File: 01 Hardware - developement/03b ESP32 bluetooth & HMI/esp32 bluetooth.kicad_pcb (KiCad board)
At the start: 2 copper layers, 152.4 x 142.2 mm, 115 parts, among them J1 I2C, J2 UART, J3 power supply, J4 Jtag, J5 I2S, J6 Backlight and leds, J7 to stepper motor, J8 Conn_01x01_Pin, Q1 BC817, Q2 BSS138, Q3 BSS138, Q4 BSS138, SW1 SW_Push_Dual, SW10 Strapping button, SW2 SW_Push_Dual, SW3 SW_Push_Dual, SW4 SW_Push_Dual, SW5 SW_Push_Dual, SW6 Rotary_Encoder_Switch, SW7 Rotary_Encoder_Switch, SW8 Strapping button, SW9 Strapping button, U1 DRV8825_STEPPER_MOTOR_DRIVER_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, U2 ESP32-DevKitC, U3 MCP23008

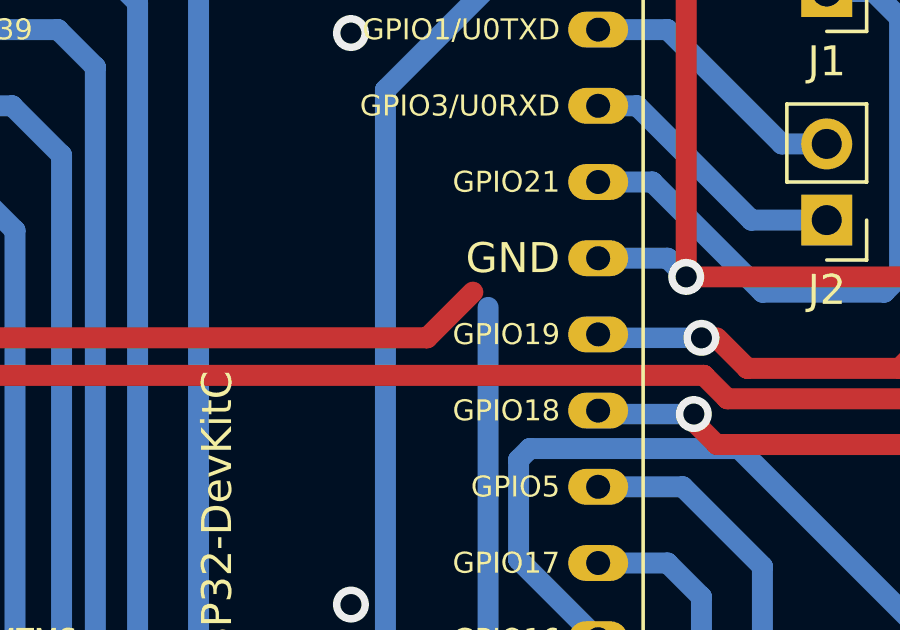
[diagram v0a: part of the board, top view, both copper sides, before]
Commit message: hw and esp32 fw inprovements GOLDEN SAMPLE, restore point
- hw - poprawiono footprinty modułów i zamieniono mux select na power supply sustain pin
- fw - poprawiono kalsę StepperOptoPowerOFF
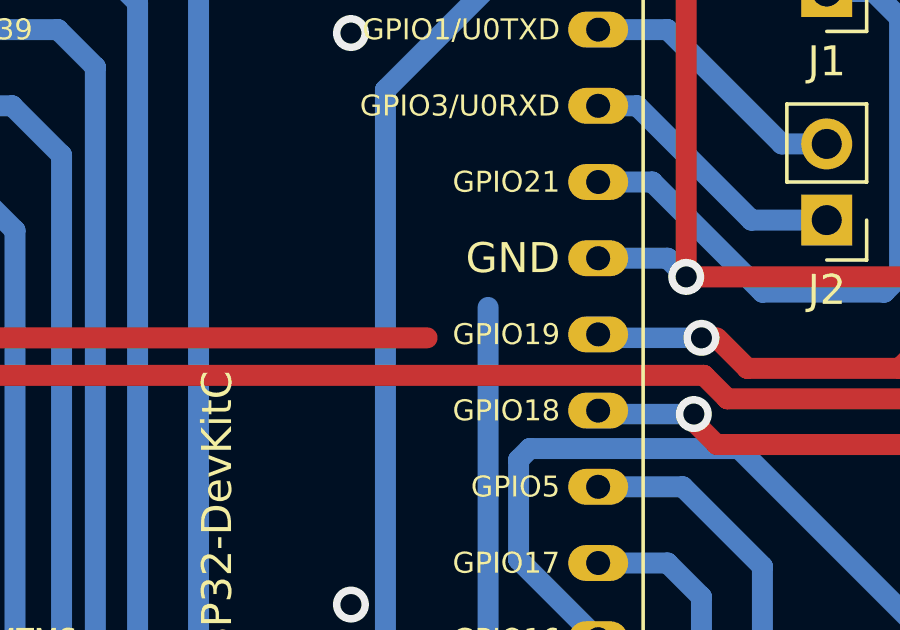
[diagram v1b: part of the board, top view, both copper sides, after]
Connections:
- net /MUX_select renamed /~{PS_Sust_ESP32}
- J5 pad 4: /I2S_MCLK -> unconnected-(J5-Pin_4-Pad4)
- J8 pad 1: Net-(J8-Pin_1) -> unconnected-(J8-Pin_1-Pad1)
- R52 pad 2: Net-(J8-Pin_1) -> unconnected-(J8-Pin_1-Pad1)
- U3 pad 8: Net-(J8-Pin_1) -> unconnected-(J8-Pin_1-Pad1)
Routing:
- net /I2S_MCLK: track 37.1 -> 0.00 mm, vias 1 -> 0
- net unconnected-(J5-Pin_4-Pad4): track 0.00 -> 34.9 mm, vias 0 -> 1
- net unconnected-(J8-Pin_1-Pad1): track 0.00 -> 11.5 mm
- net Net-(J8-Pin_1): track 11.5 -> 0.00 mm
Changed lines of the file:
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@@
   (net 19 "/I2C0_SDA")
   (net 20 "/I2C0_SCL")
-  (net 21 "/I2S_MCLK")
+  (net 21 "unconnected-(J5-Pin_4-Pad4)")
   (net 22 "/BT_UATR_RX")
   (net 23 "/BT_UATR_TX")
@@
   (net 35 "/I2S_LRCLK")
   (net 36 "/BOOT")
-  (net 37 "/MUX_select")
+  (net 37 "/~{PS_Sust_ESP32}")
   (net 38 "+5V")
   (net 39 "Net-(J6-Pin_3)")
@@
   (net 61 "Net-(R33-Pad2)")
   (net 62 "Net-(R35-Pad2)")
-  (net 63 "Net-(J8-Pin_1)")
+  (net 63 "unconnected-(J8-Pin_1-Pad1)")
   (net 64 "Net-(R39-Pad2)")
   (net 65 "/~{MotorSleep}")
@@
       (net 35 "/I2S_LRCLK") (pinfunction "Pin_3") (pintype "passive"))
     (pad "4" thru_hole oval (at 0 7.62) (size 1.7 1.7) (drill 1) (layers "*.Cu" "*.Mask")
-      (net 21 "/I2S_MCLK") (pinfunction "Pin_4") (pintype "passive"))
+      (net 21 "unconnected-(J5-Pin_4-Pad4)") (pinfunction "Pin_4") (pintype "passive+no_connect"))
     (pad "5" thru_hole oval (at 0 10.16) (size 1.7 1.7) (drill 1) (layers "*.Cu" "*.Mask")
-      (net 37 "/MUX_select") (pinfunction "Pin_5") (pintype "passive"))
+      (net 37 "/~{PS_Sust_ESP32}") (pinfunction "Pin_5") (pintype "passive"))
     (model "${KICAD6_3DMODEL_DIR}/Connector_PinHeader_2.54mm.3dshapes/PinHeader_1x05_P2.54mm_Vertical.wrl"
       (offset (xyz 0 0 0))
@@
       (net 91 "unconnected-(U3-NC-Pad7)") (pinfunction "NC") (pintype "no_connect"))
     (pad "8" smd roundrect (at -4.65 3.81) (size 2.05 0.6) (layers "F.Cu" "F.Paste" "F.Mask") (roundrect_rratio 0.25)
-      (net 63 "Net-(J8-Pin_1)") (pinfunction "INT") (pintype "output"))
+      (net 63 "unconnected-(J8-Pin_1-Pad1)") (pinfunction "INT") (pintype "output"))
     (pad "9" smd roundrect (at -4.65 5.08) (size 2.05 0.6) (layers "F.Cu" "F.Paste" "F.Mask") (roundrect_rratio 0.25)
       (net 2 "GNDD") (pinfunction "VSS") (pintype "power_in"))
     (pad "10" smd roundrect (at 4.65 5.08) (size 2.05 0.6) (layers "F.Cu" "F.Paste" "F.Mask") (roundrect_rratio 0.25)
-      (net 85 "unconnected-(U3-GP0-Pad10)") (pinfunction "GP0") (pintype "bidirectional"))
+      (net 85 "unconnected-(U3-GP0-Pad10)") (pinfunction "GP0") (pintype "bidirectional+no_connect"))
     (pad "11" smd roundrect (at 4.65 3.81) (size 2.05 0.6) (layers "F.Cu" "F.Paste" "F.Mask") (roundrect_rratio 0.25)
       (net 84 "Net-(U3-GP1)") (pinfunction "GP1") (pintype "bidirectional"))
@@
       (stroke (width 0.1) (type solid)) (layer "F.Fab"))
     (pad "1" thru_hole rect (at 0 0) (size 1.7 1.7) (drill 1) (layers "*.Cu" "*.Mask")
-      (net 63 "Net-(J8-Pin_1)") (pinfunction "Pin_1") (pintype "passive"))
+      (net 63 "unconnected-(J8-Pin_1-Pad1)") (pinfunction "Pin_1") (pintype "passive"))
     (model "${KICAD6_3DMODEL_DIR}/Connector_PinHeader_2.54mm.3dshapes/PinHeader_1x01_P2.54mm_Vertical.wrl"
       (offset (xyz 0 0 0))
@@
       (net 47 "+3V3") (pintype "passive"))
     (pad "2" smd roundrect (at 0.825 0 180) (size 0.8 0.95) (layers "B.Cu" "B.Paste" "B.Mask") (roundrect_rratio 0.25)
-      (net 63 "Net-(J8-Pin_1)") (pintype "passive"))
+      (net 63 "unconnected-(J8-Pin_1-Pad1)") (pintype "passive"))
     (model "${KICAD6_3DMODEL_DIR}/Resistor_SMD.3dshapes/R_0603_1608Metric.wrl"
       (offset (xyz 0 0 0))
@@
       (net 84 "Net-(U3-GP1)") (pintype "passive"))
     (pad "2" smd roundrect (at 0.825 0 180) (size 0.8 0.95) (layers "B.Cu" "B.Paste" "B.Mask") (roundrect_rratio 0.25)
-      (net 37 "/MUX_select") (pintype "passive"))
+      (net 37 "/~{PS_Sust_ESP32}") (pintype "passive"))
     (model "${KICAD6_3DMODEL_DIR}/Resistor_SMD.3dshapes/R_0603_1608Metric.wrl"
       (offset (xyz 0 0 0))
@@
   (segment (start 111.875 86.245) (end 113.145 84.975) (width 0.7) (layer "B.Cu") (net 20))
   (segment (start 109.84 86.245) (end 111.875 86.245) (width 0.7) (layer "B.Cu") (net 20))
-  (segment (start 105.664 97.536) (end 104.14 99.06) (width 0.7) (layer "F.Cu") (net 21))
   (segment (start 104.14 99.06) (end 88.9 99.06) (width 0.7) (layer "F.Cu") (net 21))
   (segment (start 87.503 97.663) (end 74.803 97.663) (width 0.7) (layer "F.Cu") (net 21))

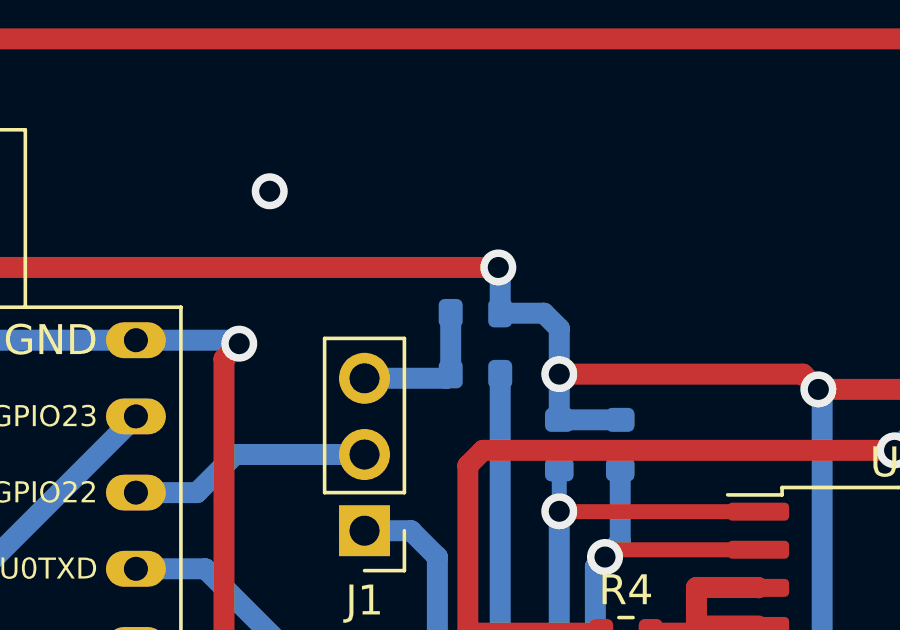
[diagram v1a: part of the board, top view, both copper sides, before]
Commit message: ESP32 bluetooth & HMI -HW- interrupt request pull-down
Zmieniono R57 - pierwotnie rezystor ten był PULL-UP na linii i2cItterrupt request teraz jest PULL-DOWN
Zmiana jest po to, aby wykryć start ESp32. Po zboot'owaniu się ESP32 gaje sygnał na tej linii UP
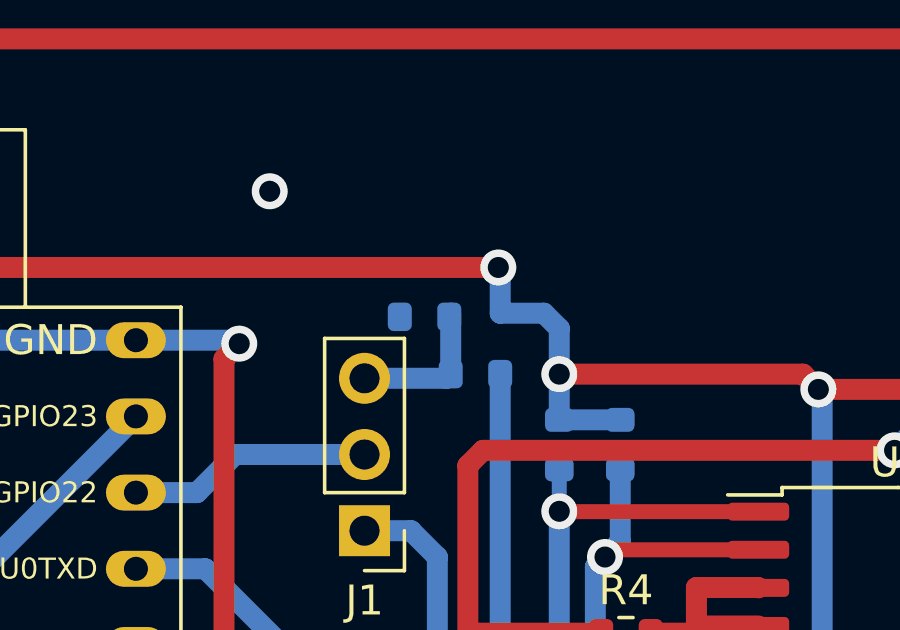
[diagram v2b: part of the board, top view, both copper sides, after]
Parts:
- moved R57 1.70 mm to (119.5, 80.4), turned to 180 degrees
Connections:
- R57 pad 2: +3V3 -> GNDD
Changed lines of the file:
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@@
   )
   (footprint "Resistor_SMD:R_0603_1608Metric" (layer "B.Cu")
-    (at 121.158 80.264)
+    (at 119.460595 80.384893 180)
     (descr "Resistor SMD 0603 (1608 Metric), square (rectangular) end terminal, IPC_7351 nominal, (Body size source: IPC-SM-782 page 72, https://www.pcb-3d.com/wordpress/wp-content/uploads/ipc-sm-782a_amendment_1_and_2.pdf), generated with kicad-footprint-generator")
     (tags "resistor")
@@
     (fp_line (start 0.8 0.4125) (end 0.8 -0.4125)
       (stroke (width 0.1) (type solid)) (layer "B.Fab"))
-    (pad "1" smd roundrect (at -0.825 0) (size 0.8 0.95) (layers "B.Cu" "B.Paste" "B.Mask") (roundrect_rratio 0.25)
+    (pad "1" smd roundrect (at -0.825 0 180) (size 0.8 0.95) (layers "B.Cu" "B.Paste" "B.Mask") (roundrect_rratio 0.25)
       (net 95 "Net-(J1-Pin_3)") (pintype "passive"))
-    (pad "2" smd roundrect (at 0.825 0) (size 0.8 0.95) (layers "B.Cu" "B.Paste" "B.Mask") (roundrect_rratio 0.25)
-      (net 47 "+3V3") (pintype "passive"))
+    (pad "2" smd roundrect (at 0.825 0 180) (size 0.8 0.95) (layers "B.Cu" "B.Paste" "B.Mask") (roundrect_rratio 0.25)
+      (net 2 "GNDD") (pintype "passive"))
     (model "${KICAD6_3DMODEL_DIR}/Resistor_SMD.3dshapes/R_0603_1608Metric.wrl"
       (offset (xyz 0 0 0))

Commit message: Do poprwy jest schemat rotary encodera
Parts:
- added D10: ESD5Z3.3T1G, Diode_SMD:D_SOD-523, F.Cu at (-64.0, 106.2)
- added D11: ESD5Z3.3T1G, Diode_SMD:D_SOD-523, F.Cu at (-64.0, 108.7)
- added D12: ESD5Z3.3T1G, Diode_SMD:D_SOD-523, F.Cu at (-64.0, 111.1)
- added D5: ESD5Z3.3T1G, Diode_SMD:D_SOD-523, F.Cu at (-64.0, 94.0)
- added D6: ESD5Z3.3T1G, Diode_SMD:D_SOD-523, F.Cu at (-64.0, 96.4)
- added D7: ESD5Z3.3T1G, Diode_SMD:D_SOD-523, F.Cu at (-64.0, 98.8)
- added D8: ESD5Z3.3T1G, Diode_SMD:D_SOD-523, F.Cu at (-64.0, 101.3)
- added D9: ESD5Z3.3T1G, Diode_SMD:D_SOD-523, F.Cu at (-64.0, 103.8)
- added ESP-Prog1: Conn_02x03_Odd_Even, Connector_IDC:IDC-Header_2x03_P2.54mm_Vertical, F.Cu at (-57.0, 98.8)
- added J10: Conn_01x02_Pin, Connector_PinHeader_1.27mm:PinHeader_1x02_P1.27mm_Vertical, F.Cu at (-60.1, 111.7)
- added J11: Conn_01x02_Pin, Connector_PinHeader_1.27mm:PinHeader_1x02_P1.27mm_Vertical, F.Cu at (-56.0, 111.7)
- added J9: Conn_02x05_Odd_Even, Connector_IDC:IDC-Header_2x05_P2.54mm_Vertical, F.Cu at (-72.6, 98.8)
